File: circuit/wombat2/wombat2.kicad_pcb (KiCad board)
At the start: 2 copper layers, 137.1 x 85 mm, 136 parts, among them J1 Conn_01x04_Pin, J2 Conn_01x04_Pin, Q1 IXTA10P50P, Q10 IPB95R130PFD7ATMA1, Q2 IXTA10P50P, Q9 IPB95R130PFD7ATMA1, U1 2EDN7524FXTMA1, U10 LD1117S33TR_SOT223, U2 L7805, U3 2EDN7524FXTMA1, U4 TMUX1108PW, U5 TSB7191A, U6 TSB7191A, U7 ADS1115IDGS, U9 XIAO-ESP32-C3-SMD

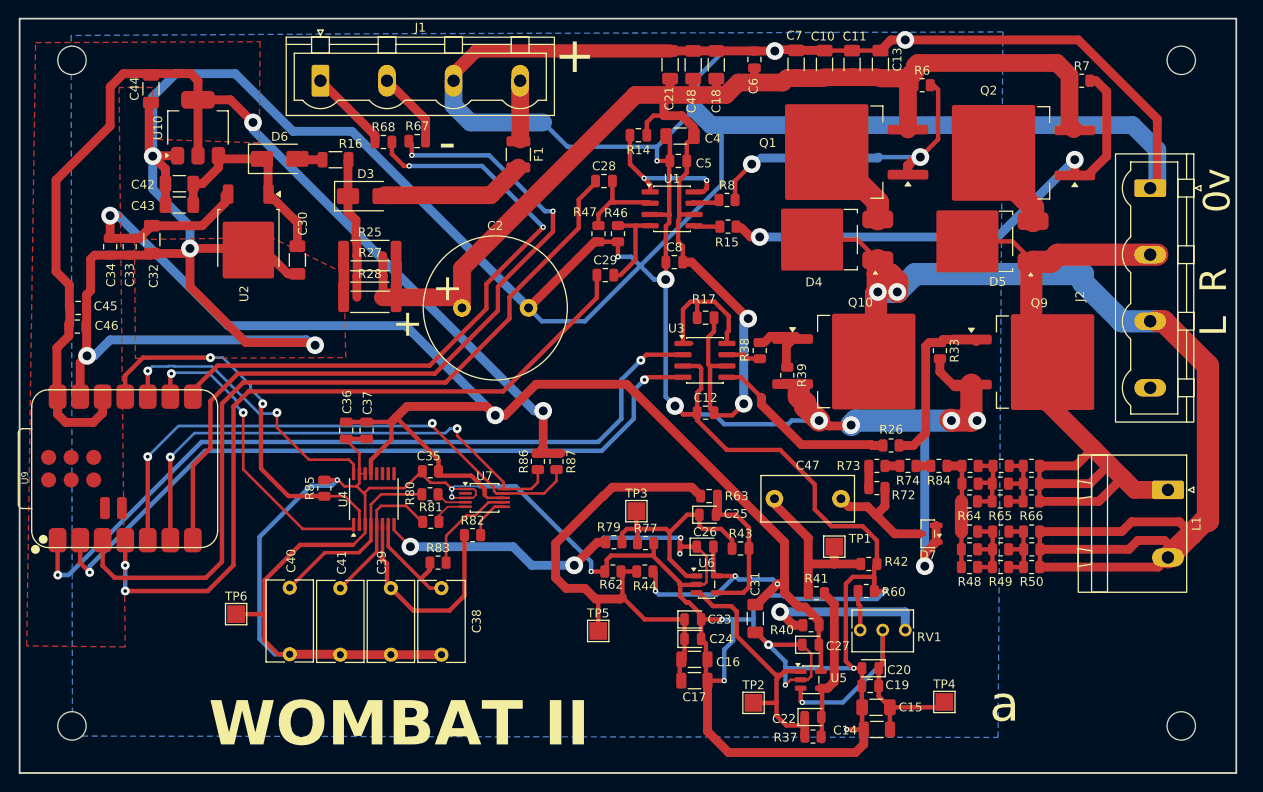
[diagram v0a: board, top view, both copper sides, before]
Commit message: Update KiCad schematic/PCB; track custom footprint library
- Whitelist Library.pretty/*.kicad_mod in the circuit .gitignore so the
  custom footprints are versioned (symbol libs / fp-lib-table still excluded)
- Update schematic, PCB, and project file

Co-Authored-By: Claude Opus 4.8 (1M context) <noreply@anthropic.com>
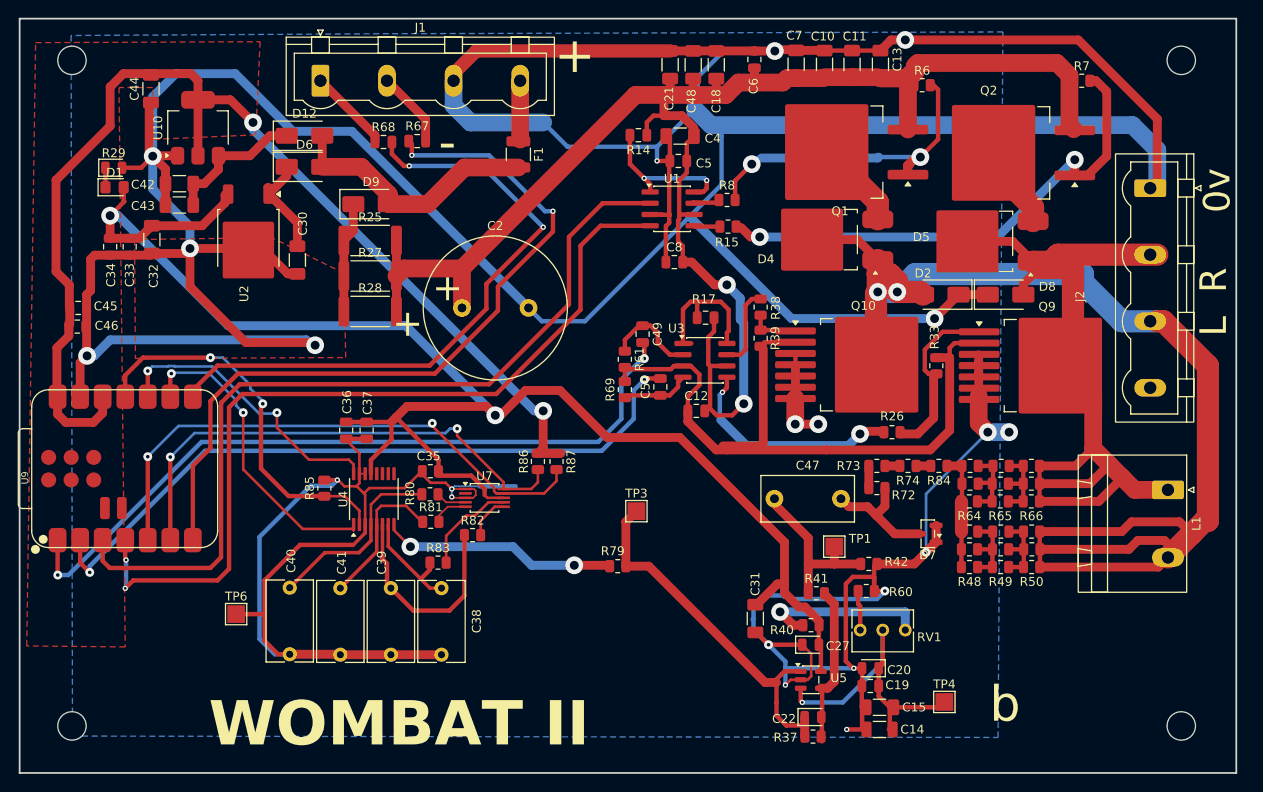
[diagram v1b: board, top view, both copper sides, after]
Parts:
- removed C16, C17: 10uF, Capacitor_SMD:C_1206_3216Metric
- removed C23: 1uF, LED_SMD:LED_0805_2012Metric
- removed C24, C26: 0.1uF, LED_SMD:LED_0805_2012Metric
- removed C25: 47pF, LED_SMD:LED_0805_2012Metric
- removed C28, C29: 1uF, Capacitor_SMD:C_0805_2012Metric
- removed D3: 1N5819WS, Diode_SMD:D_SMA
- removed R16: 1, Resistor_SMD:R_1206_3216Metric
- removed R43: 33k, Capacitor_SMD:C_0805_2012Metric
- removed R44, R62: 1k, Resistor_SMD:R_0805_2012Metric
- removed R46, R47, R77: 10k, Resistor_SMD:R_0805_2012Metric
- removed R63: 270, Capacitor_SMD:C_0805_2012Metric
- removed TP2, TP5: TestPoint, TestPoint:TestPoint_Pad_2.0x2.0mm
- removed U6: TSB7191A, Package_TO_SOT_SMD:SOT-23-5
- added C49: 1uF, Capacitor_SMD:C_0805_2012Metric, F.Cu at (163.3, 71.8)
- added C50: 1uF, Capacitor_SMD:C_0805_2012Metric, F.Cu at (165.3, 77.8)
- added D1: LED, LED_SMD:LED_0805_2012Metric_Pad1.15x1.40mm_HandSolder, F.Cu at (103.8, 55.3)
- added D12: 1N5819WS, Diode_SMD:D_SMA, F.Cu at (125.2, 49.5)
- added D2: TPSMB600CA-A, Diode_SMD:D_SMA, F.Cu at (196.9, 67.4)
- added D8: TPSMB600CA-A, Diode_SMD:D_SMA, F.Cu at (204.2, 67.4)
- added D9: 1N5819WS, Diode_SMD:D_SMA, F.Cu at (132.7, 57.2)
- added R29: 1k, LED_SMD:LED_0805_2012Metric, F.Cu at (103.7, 53.1)
- added R61: 10k, Resistor_SMD:R_0805_2012Metric, F.Cu at (161.3, 74.7)
- added R69: 10k, Resistor_SMD:R_0805_2012Metric, F.Cu at (161.3, 78.1)
- Q1, Q2: value IXTA10P50P -> STD35P6LLF6
- Q10, Q9: value IPB95R130PFD7ATMA1 -> IMBG120R234M2HXTMA1; footprint Package_TO_SOT_SMD:TO-263-2 -> wombat:TO-263-7_TabPin4
- R15, R26, R38, R8: value 10 -> 2.7 ohm
- R41: value 10k -> 270
- moved R39 5.14 mm to (176.6, 72.3)
- moved R38 4.91 mm to (176.6, 68.8), turned to 90 degrees
- moved D6 2.94 mm to (125.2, 53.0)
- moved R79 2.74 mm to (160.5, 98.0)
- moved R33 1.75 mm to (196.4, 75.4), turned to 90 degrees
- moved R25 1.70 mm to (132.6, 61.3)
- moved R28 1.60 mm to (132.6, 69.3)
- moved R26 1.50 mm to (191.4, 82.9)
- moved C12 1.07 mm to (169.3, 80.5)
- moved Q9 0.96 mm to (208.9, 75.4)
- moved Q10 0.49 mm to (188.2, 75.3)
- moved C15 0.40 mm to (190.0, 113.9)
- moved C14 0.30 mm to (190.0, 116.4)
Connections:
- C22 pad 1: Net-(U6-+) -> /signal
- C42 pad 2: Net-(D6-K) -> Net-(D12-K)
- C43 pad 2: Net-(D6-K) -> Net-(D12-K)
- D6 pad 2: Net-(D6-A) -> +15V
- F1 pad 2: Net-(D3-A) -> +15V
- R25 pad 1: +15V -> Net-(D9-K)
- R27 pad 1: +15V -> Net-(D9-K)
- R28 pad 1: +15V -> Net-(D9-K)
- R37 pad 2: Net-(U6-+) -> /signal
- U1 pad 2: Net-(U1-INA) -> /high_left
- U1 pad 4: Net-(U1-INB) -> /high_right
- U10 pad 3: Net-(D6-K) -> Net-(D12-K)
- U3 pad 2: /low_left -> Net-(U3-INA)
- U3 pad 4: /low_right -> Net-(U3-INB)
- U5 pad 1: Net-(U6-+) -> /signal
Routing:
- net GND: track 884.8 -> 800.2 mm, vias 28 -> 21
- net Net-(C16-Pad1): track 56.0 -> 0.00 mm
- net Net-(U6-+): track 30.9 -> 0.00 mm
- net +5V: track 199.2 -> 179.6 mm, vias 5 -> 2
- net Net-(U6--): track 17.1 -> 0.00 mm
- net Net-(D12-K): track 0.00 -> 16.6 mm
- net Net-(D3-A): track 16.5 -> 0.00 mm
- net /signal: track 27.9 -> 42.4 mm
- net +15V: track 16.0 -> 29.7 mm
- net Net-(D9-K): track 0.00 -> 12.5 mm
- net /COIL_RIGHT: track 87.0 -> 99.0 mm
- net Net-(D6-K): track 23.9 -> 11.9 mm
- net /high_right: track 85.6 -> 96.5 mm
- net Net-(U1-INB): track 10.6 -> 0.00 mm
- net Net-(U3-INA): track 0.00 -> 10.5 mm
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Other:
- board text added: "b"
- board text removed: "a"

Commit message: Add XIAO-ESP32-C3 footprint with 3D model; update board and schematic
- Add XIAO-ESP32-C3-DIP-SMD footprint to the wombat library (3D model attached)
- Repoint the board's XIAO to the wombat-library footprint
- Update schematic and PCB

Co-Authored-By: Claude Opus 4.8 (1M context) <noreply@anthropic.com>
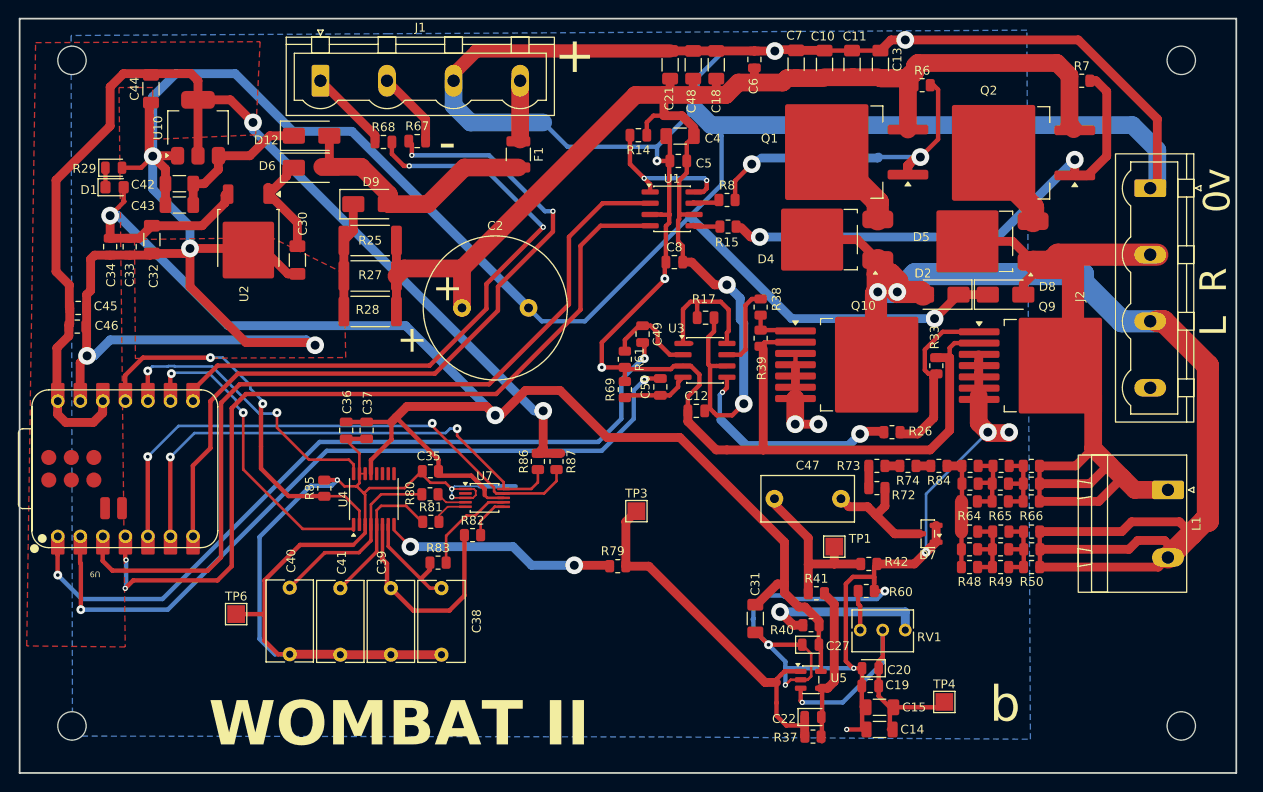
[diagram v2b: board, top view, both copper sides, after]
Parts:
- U9: footprint Seeed Studio XIAO Series Library:XIAO-ESP32-C3-SMD -> wombat:XIAO-ESP32-C3-DIP-SMD
- moved U9 13.7 mm to (105.0, 87.0), turned to 180 degrees
- moved D6 0.81 mm to (126.0, 53.1)
- moved D12 0.80 mm to (126.0, 49.5)
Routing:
- net GND: track 800.2 -> 811.9 mm, vias 21 -> 23
- net /low_right: track 79.7 -> 86.9 mm
- net /low_left: track 85.0 -> 88.5 mm
- net /S1: track 33.0 -> 36.4 mm
- net /S0: track 35.3 -> 37.7 mm
- net /high_left: track 96.0 -> 97.0 mm
- net /high_right: track 96.5 -> 97.1 mm
- net Net-(U5-+): track 35.1 -> 34.6 mm
